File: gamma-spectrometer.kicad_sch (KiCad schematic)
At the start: 45 parts, among them J1 *, J2 *, Q1 2N7002, U1 Pico 2, U3 TLV3201AIDBVR, U4 OPA357AIDBVR, U5 OPA357AIDBVR, U6 LM4040AIM3-3.0+T, U8 MAX5026EUT_T

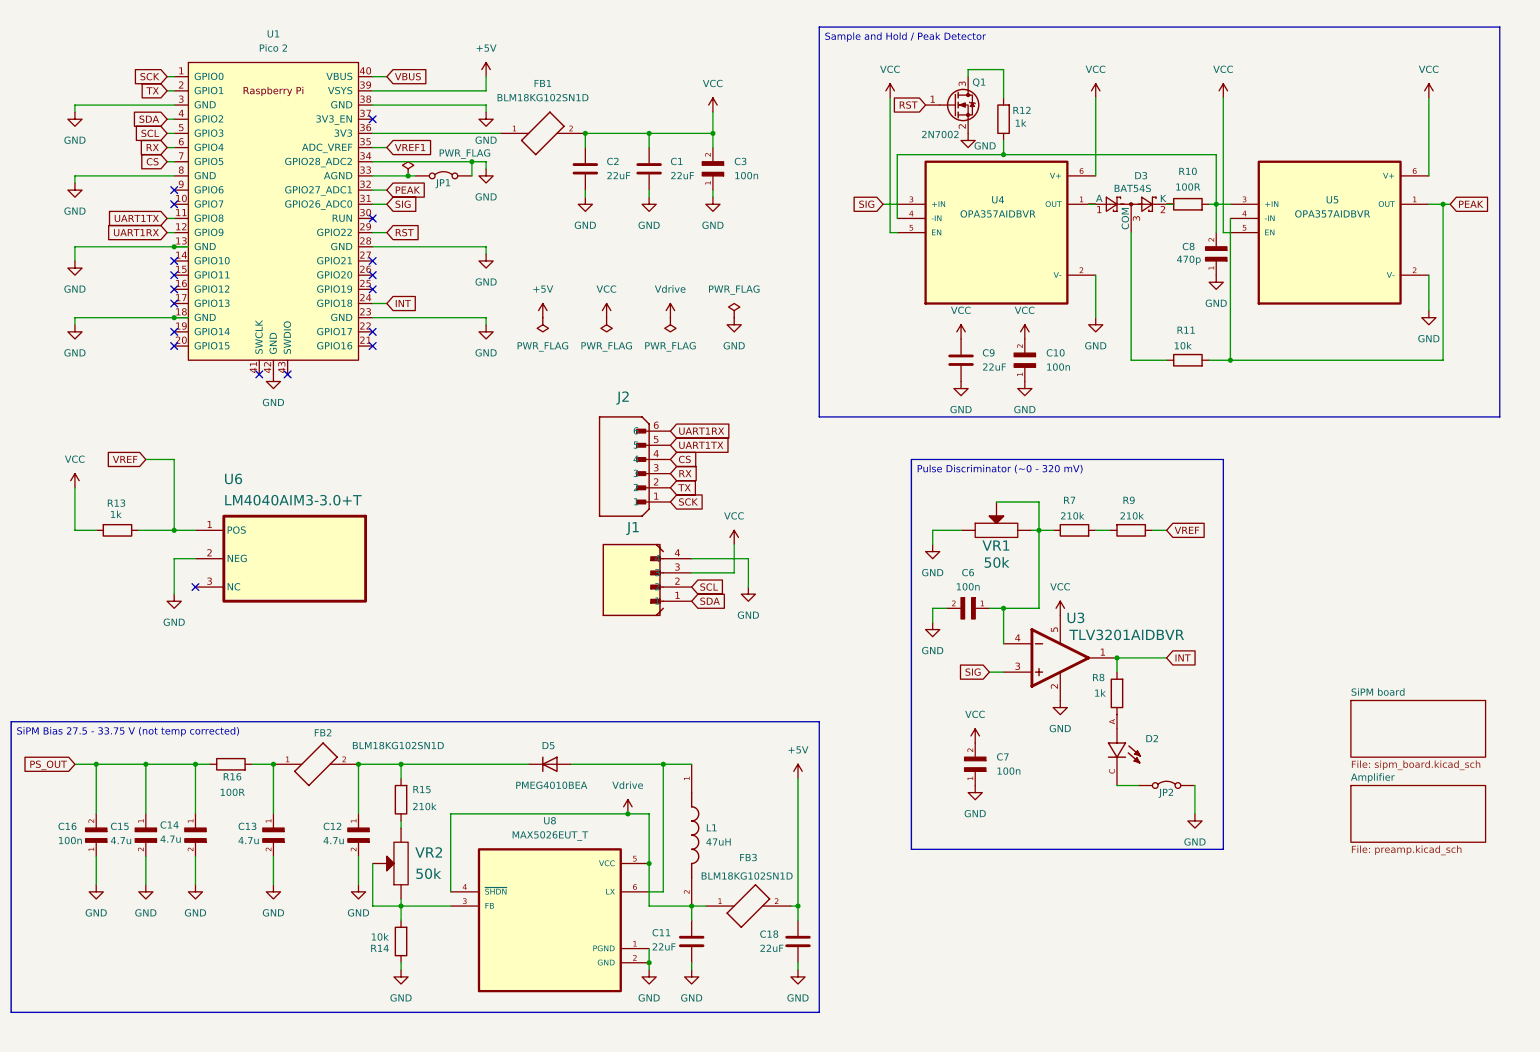
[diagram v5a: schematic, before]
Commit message: Switched to MAX1422 external ADC
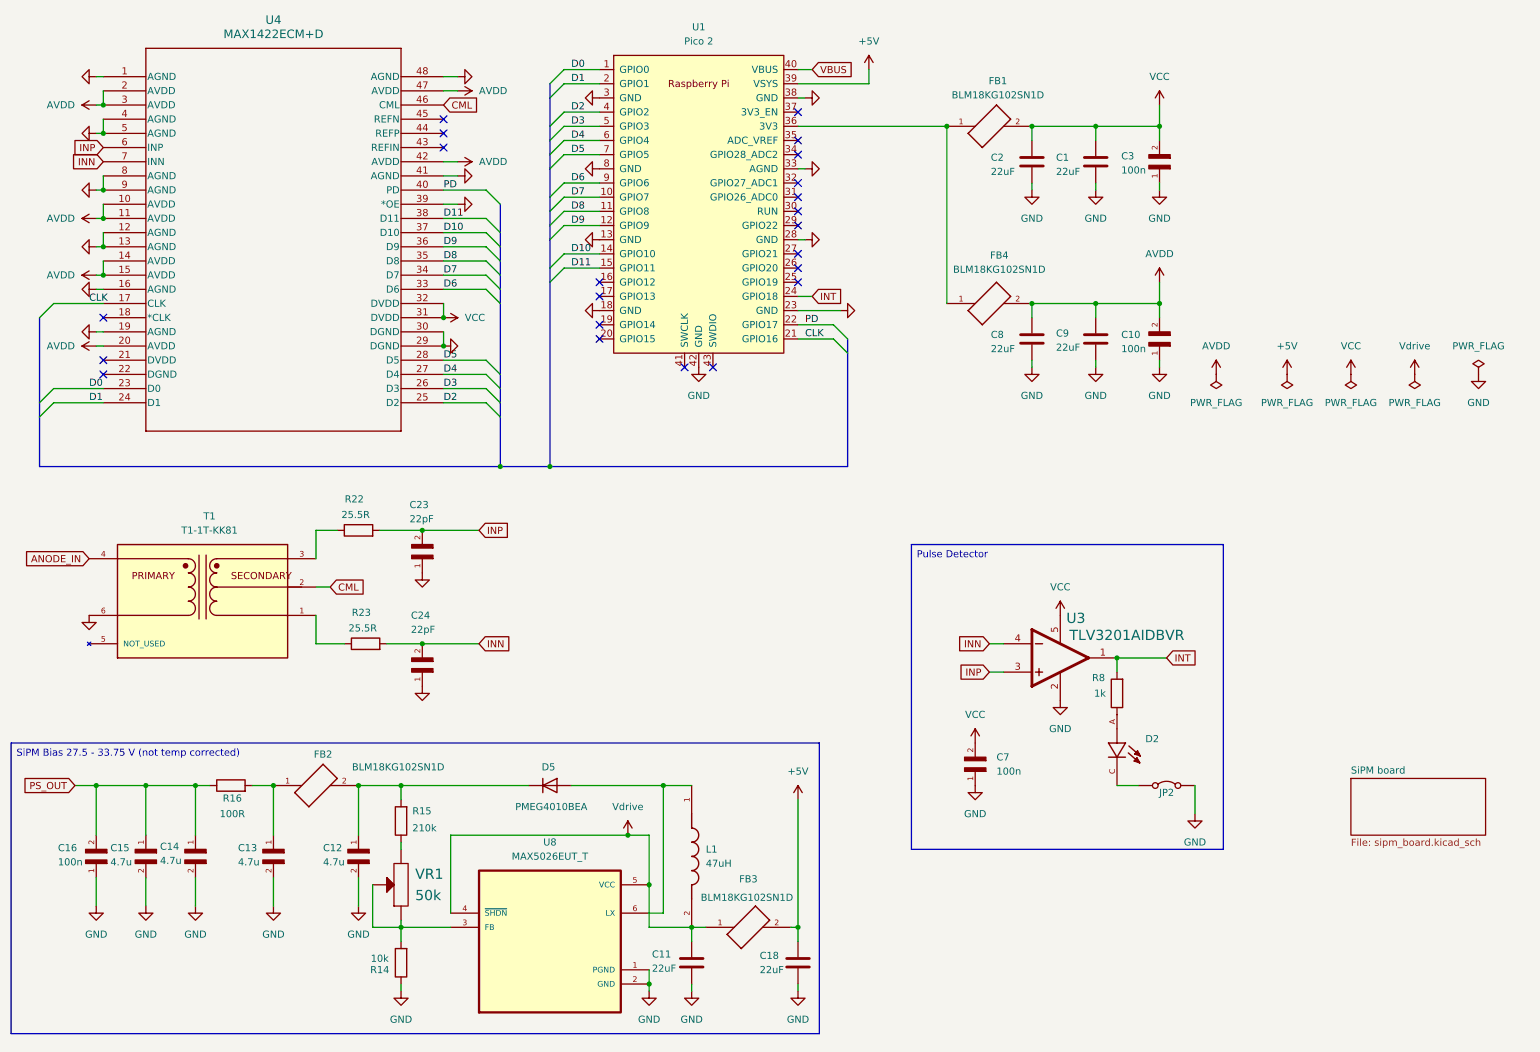
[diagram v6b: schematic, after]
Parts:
- removed C6: 100n, CL10B104KC8NNNC:CAPC1608X90N, symbol CL10B104KC8NNNC:CL10B104KC8NNNC
- removed C8: 470p, ECHU1C471JX5:CAP_ECHU1C471JX5, symbol ECHU1C471JX5:ECHU1C471JX5
- removed D3: BAT54S, Package_TO_SOT_SMD:SOT-23, symbol Diode:BAT54S
- removed J1: *, B4B-PH-K-S_LF__SN_:JST_B4B-PH-K-S(LF)(SN), symbol B4B-PH-K-S_LF__SN_:B4B-PH-K-S(LF)(SN)
- removed J2: *, B6B-PH-K-S_LF__SN_:JST_B6B-PH-K-S(LF)(SN), symbol B6B-PH-K-S_LF__SN_:B6B-PH-K-S(LF)(SN)
- removed JP1: ~, Jumper:SolderJumper-2_P1.3mm_Open_TrianglePad1.0x1.5mm, symbol Jumper:Jumper_2_Bridged
- removed Q1: 2N7002, Package_TO_SOT_SMD:SOT-23, symbol Transistor_FET:2N7002
- removed R10: 100R, ERJ3EKF1000V:RES_ERJ3EKF1000V, symbol Device:R
- removed R11: 10k, ERJ3EKF1002V:RES_ERJ3EKF1002V, symbol Device:R
- removed R12, R13: 1k, ERJ3EKF1001V:RES_ERJ3EKF1001V, symbol Device:R
- removed R7, R9: 210k, ERJ3EKF2103V:RES_ERJ3EKF2103V, symbol Device:R
- removed U4, U5: OPA357AIDBVR, OPA357AIDBVR:SOT95P280X145-6N, symbol OPA357AIDBVR:OPA357AIDBVR
- removed U6: LM4040AIM3-3.0+T, LM4040AIM3-3_0-T:SOT95P237X112-3N, symbol LM4040AIM3-3_0-T:LM4040AIM3-3_0-T
- removed VR1: 50k, 3266W-1-503:TRIM_3266W-1-503, symbol 3296W-1-503LF:3296W-1-503LF
- added C23, C24: 22pF, ECJ-1VC1H220J:CAPC1608X90N, symbol ECHU1C471JX5:ECHU1C471JX5
- added C8: 22uF, CL10A226MP8NUNE:CAPC1608X90N, symbol Device:C
- added FB4: BLM18KG102SN1D, BLM18KG102SN1D:BEADC1608X95N, symbol ACML-0402HC-301-T:ACML-0402HC-301-T
- added R22, R23: 25.5R, ERJ3EKF25R5V:RES_ERJ3EKF25R5V, symbol Device:R
- added T1: T1-1T-KK81, T1-1T-KK81:XFMR_T1-1T-KK81_, symbol T1-1T-KK81:T1-1T-KK81_
- added U4: MAX1422ECM+D, MAX1422ECM-D:21-0054G_48_MXM, symbol MAX1422:MAX1422ECM+D
- renumbered VR2 to VR1
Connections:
- net GND: now also U1.33 (AGND), C23.1, C24.1, C8.2, T1.6, U4.1 (AGND), U4.12 (AGND), U4.13 (AGND), U4.16 (AGND), U4.19 (AGND), U4.29 (DGND), U4.30 (DGND), U4.39 (*OE), U4.4 (AGND), U4.41 (AGND), U4.48 (AGND), U4.5 (AGND), U4.8 (AGND), U4.9 (AGND); no longer U1.34 (GPIO28_ADC2)
- net VCC: now also U4.31 (DVDD), U4.32 (DVDD); no longer C10.2, C9.1
- net INN: now reaches U3.4 (IN-)
- net INN: now also C24.2, R23.2, U4.7 (INN)
- net at FB1.1, U1.36 (3V3): now also FB4.1
- net D7: now reaches U1.10 (GPIO7)
- net D7: now also U4.34 (D7)
- net D10: now reaches U1.14 (GPIO10)
- net D10: now also U4.37 (D10)
- net D11: now reaches U1.15 (GPIO11)
- net D11: now also U4.38 (D11)
- net CLK: now reaches U1.21 (GPIO16)
- net CLK: now also U4.17 (CLK)
- net PD: now reaches U1.22 (GPIO17)
- net PD: now also U4.40 (PD)
- net D6: now reaches U1.9 (GPIO6)
- net D6: now also U4.33 (D6)
- net CS renamed D5
- net D5: now also U4.28 (D5)
- net PEAK: no longer names the net of U1.32 (GPIO27_ADC1)
- net RST: no longer names the net of U1.29 (GPIO22)
- net RX renamed D4
- net D4: now also U4.27 (D4)
- net SCK renamed D0
- net D0: now also U4.23 (D0)
- net SCL renamed D3
- net D3: now also U4.26 (D3)
- net SDA renamed D2
- net D2: now also U4.25 (D2)
- net SIG: no longer names the net of U1.31 (GPIO26_ADC0)
- net SIG: no longer U3.3 (IN+)
- net TX renamed D1
- net D1: now also U4.24 (D1)
- net UART1RX renamed D9
- net D9: now also U4.36 (D9)
- net UART1TX renamed D8
- net D8: now also U4.35 (D8)
- net VREF1: no longer names the net of U1.35 (ADC_VREF)
- new net: R22.1, T1.3
- new net: R23.1, T1.1
- new net ANODE_IN: T1.4
- new net AVDD: C10.2, C8.1, C9.1, FB4.2, U4.10 (AVDD), U4.11 (AVDD), U4.14 (AVDD), U4.15 (AVDD), U4.2 (AVDD), U4.20 (AVDD), U4.3 (AVDD), U4.42 (AVDD), U4.47 (AVDD)
- new net CML: T1.2, U4.46 (CML)
- new net INP: C23.2, R22.2, U3.3 (IN+), U4.6 (INP)
- no-connect marks 18 -> 22
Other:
- removed sheet Amplifier
- moved on the sheet: C1, C11, C12, C13, C14, C15, C16, C18, C2, C3, D5, FB1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

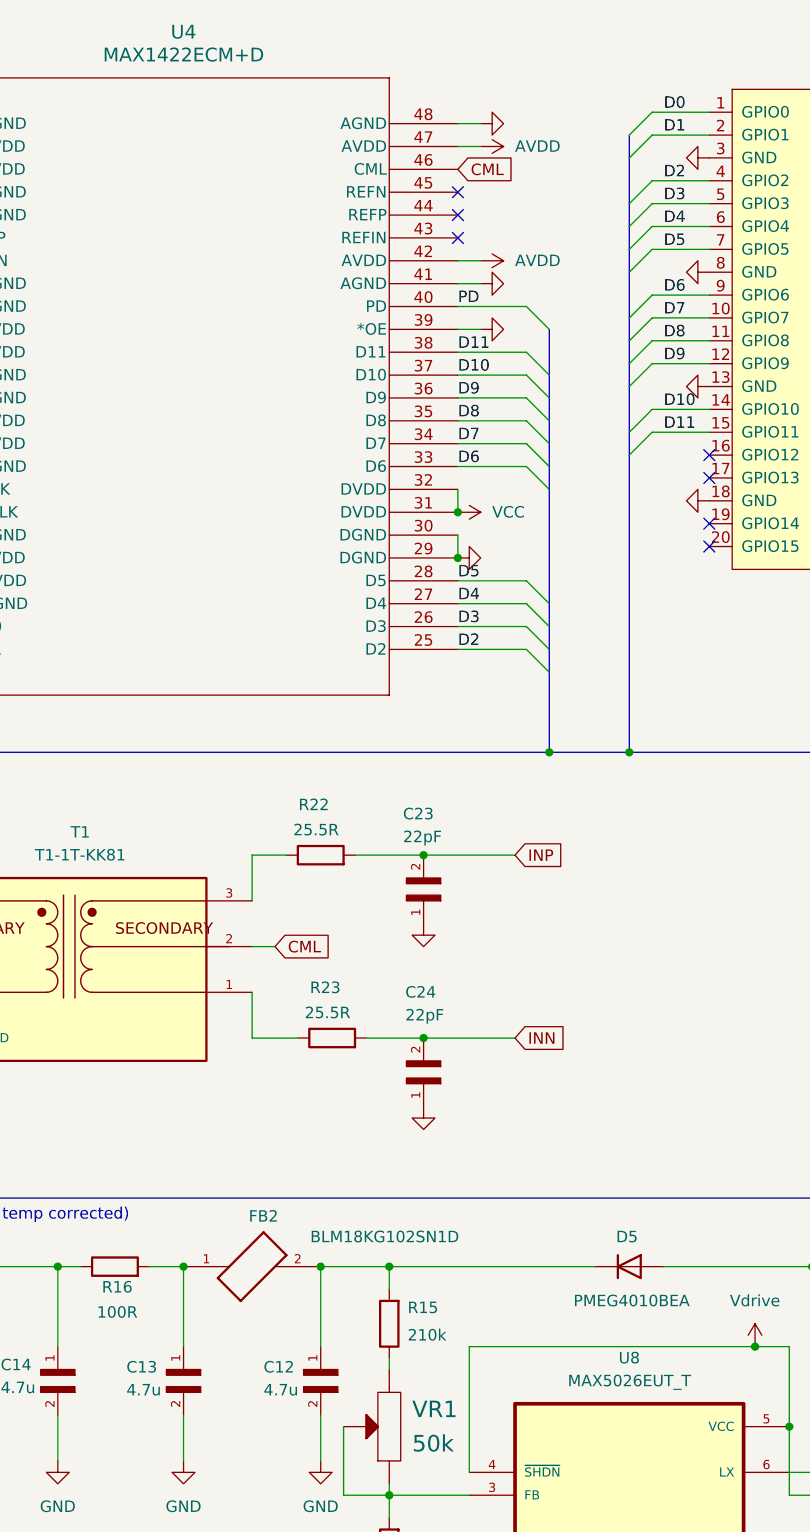
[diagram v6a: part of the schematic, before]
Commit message: Updated 3d models
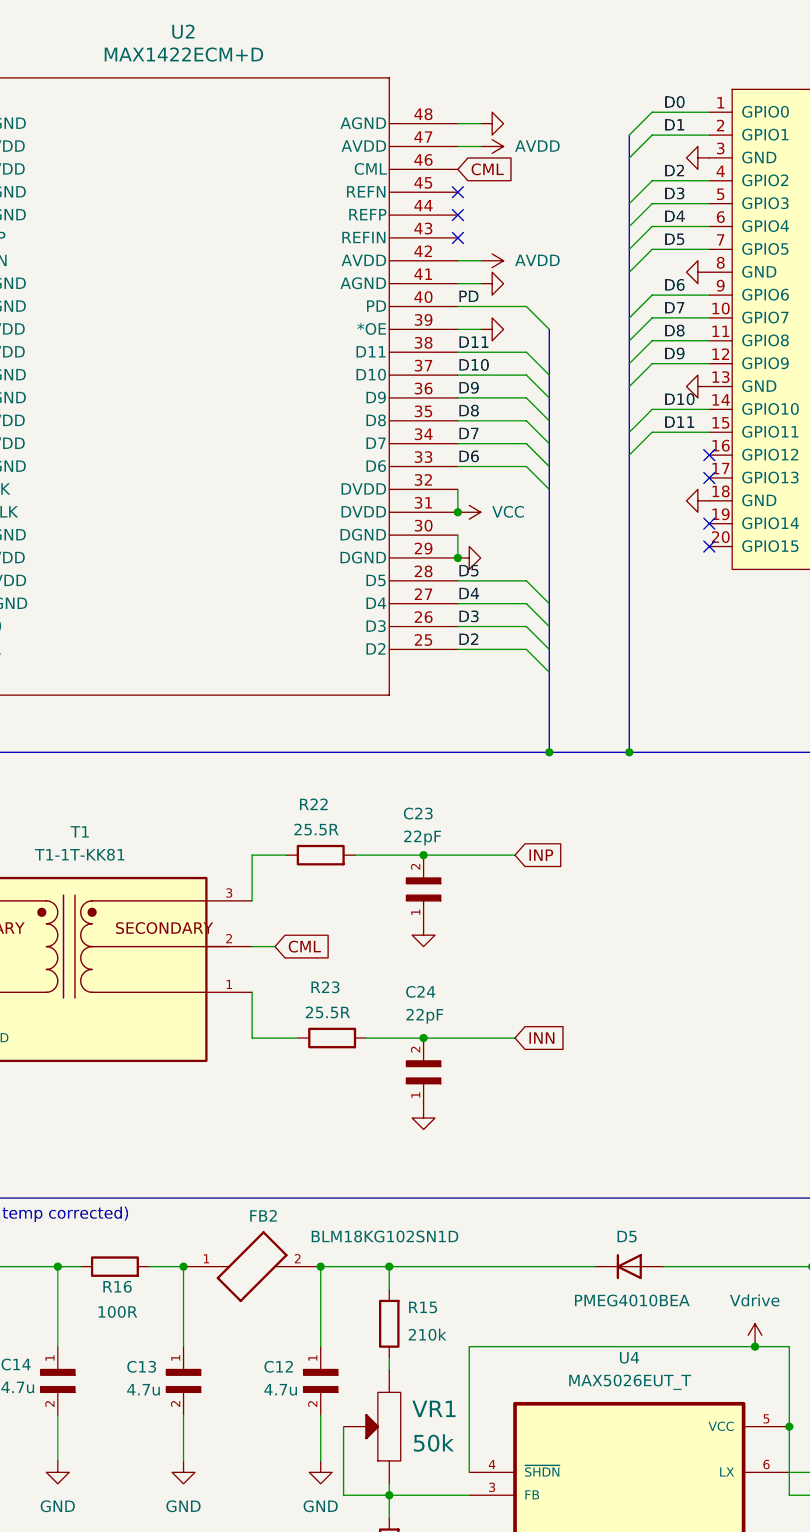
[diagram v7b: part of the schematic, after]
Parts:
- renumbered U4 to U2, U8 to U4
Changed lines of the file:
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@@
 		(on_board yes)
 		(dnp no)
-		(property "Reference" "U4"
+		(property "Reference" "U2"
 			(at 63.5 13.97 0)
 			(effects
@@
 			(project ""
 				(path "/1fc9c372-472b-46ca-8d3b-f4aefe31a8be"
-					(reference "U4")
+					(reference "U2")
 					(unit 1)
 				)
@@
 		(dnp no)
 		(fields_autoplaced yes)
-		(property "Reference" "U8"
+		(property "Reference" "U4"
 			(at 113.03 161.29 0)
 			(effects
@@
 			(project ""
 				(path "/1fc9c372-472b-46ca-8d3b-f4aefe31a8be"
-					(reference "U8")
+					(reference "U4")
 					(unit 1)
 				)
